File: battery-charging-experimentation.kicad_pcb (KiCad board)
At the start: 2 copper layers, 37 x 22.5 mm, 21 parts, among them J1 USB_C_Receptacle_PowerOnly_6P, Q1 FS8205A, Q2 AO3415A, U2 DW01, U3 TP4056-42-ESOP8

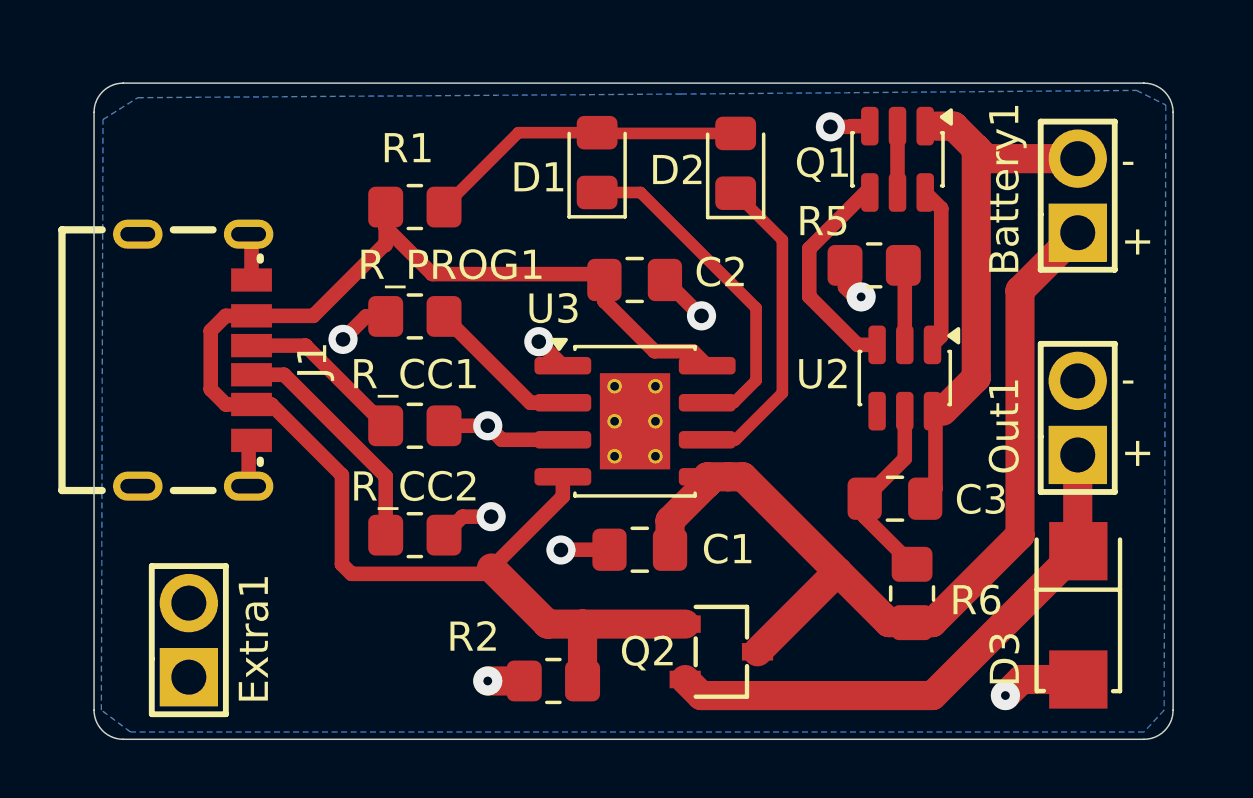
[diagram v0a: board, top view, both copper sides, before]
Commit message: move diode so the thing actually works
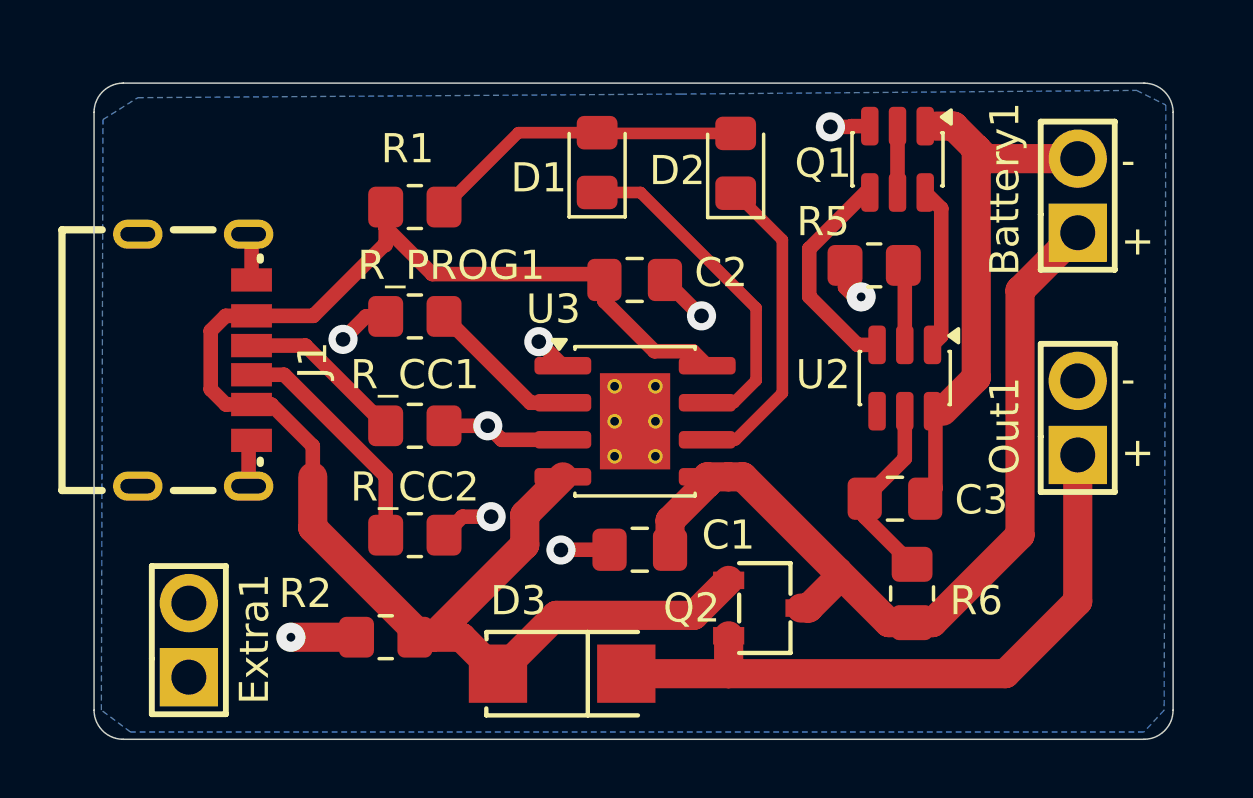
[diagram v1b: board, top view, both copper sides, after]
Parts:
- moved D3 17.8 mm to (69.5, 67.8), turned to 180 degrees
- moved R2 5.94 mm to (63.5, 66.5)
- moved Q2 2.11 mm to (76.5, 65.5)
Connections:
- D3 pad 2: GND -> /VBUS
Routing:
- net /VBUS: track 52.3 -> 57.5 mm
- net /VBUS or BATT+: track 19.1 -> 22.8 mm
- net BATT+: track 32.1 -> 30.2 mm
- net GND: track 22.5 -> 20.8 mm, vias 10 -> 9

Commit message: add a vbus out pin
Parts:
- Out1: footprint easyeda2kicad:HDR-TH_2P-P2.54-V-M -> Connector_PinHeader_2.54mm:PinHeader_1x03_P2.54mm_Vertical
- moved Out1 1.27 mm to (87.2, 60.2), turned to 0 degrees
- moved D3 0.87 mm to (70.0, 67.0)
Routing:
- net /VBUS: track 57.5 -> 78.5 mm
- net /VBUS or BATT+: track 22.8 -> 20.9 mm
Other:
- board text added: "B"
- board text added: "chargey board v2.0"
- board text removed: "chargey board v1.0"

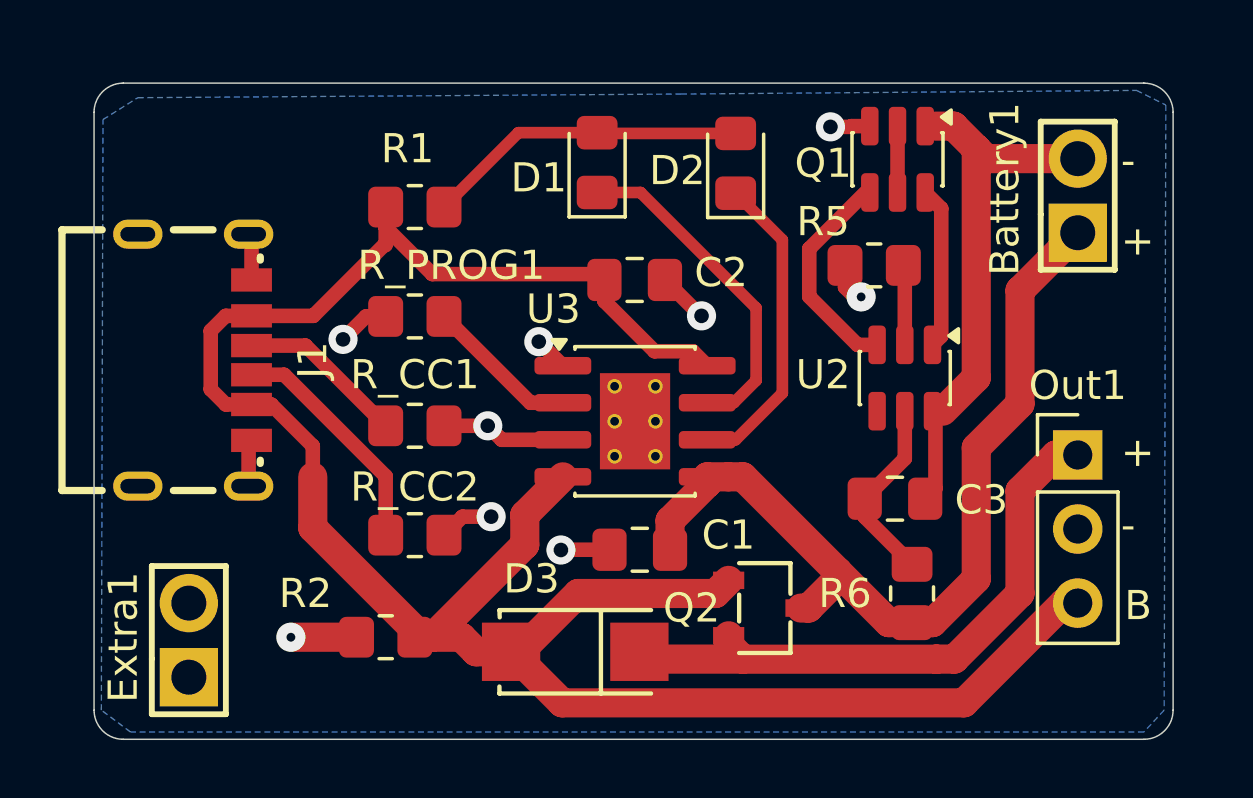
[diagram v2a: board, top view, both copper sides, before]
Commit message: smaller components, power from pico USB port
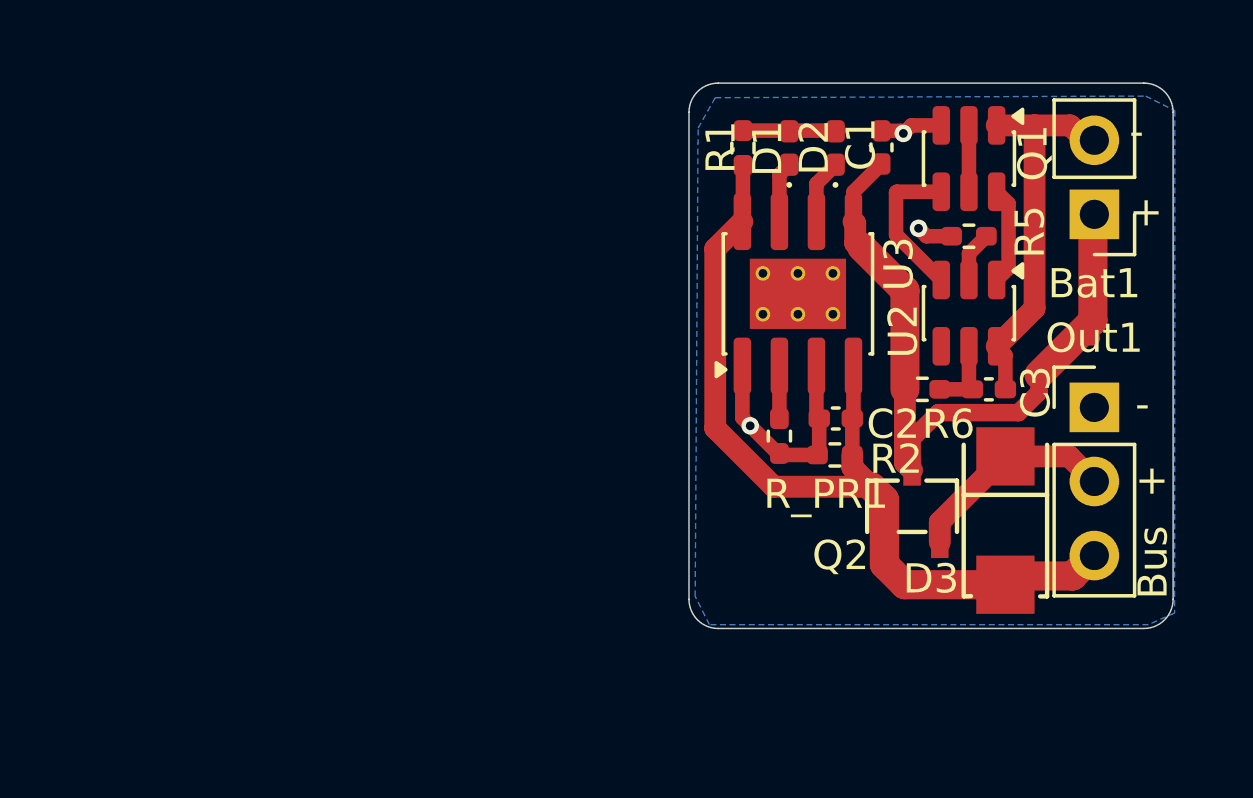
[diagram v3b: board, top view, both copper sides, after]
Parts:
- removed Battery1, Extra1: Header, easyeda2kicad:HDR-TH_2P-P2.54-V-M
- removed J1: USB_C_Receptacle_PowerOnly_6P, easyeda2kicad:USB-C-SMD
- removed R_CC1, R_CC2: 5.1k, Resistor_SMD:R_0805_2012Metric_Pad1.20x1.40mm_HandSolder
- removed R_PROG1: 1.2k, Resistor_SMD:R_0805_2012Metric_Pad1.20x1.40mm_HandSolder
- added Bat1: Conn_01x02_Pin, Connector_PinHeader_2.54mm:PinHeader_1x02_P2.54mm_Vertical, F.Cu at (87.8, 52.0)
- added R_PR1: 1.2k, Resistor_SMD:R_0402_1005Metric_Pad0.72x0.64mm_HandSolder, F.Cu at (77.0, 59.6)
- C1, C2, C3: footprint Capacitor_SMD:C_0805_2012Metric_Pad1.18x1.45mm_HandSolder -> Capacitor_SMD:C_0402_1005Metric_Pad0.74x0.62mm_HandSolder
- D1, D2: footprint LED_SMD:LED_0805_2012Metric_Pad1.15x1.40mm_HandSolder -> LED_SMD:LED_0402_1005Metric_Pad0.77x0.64mm_HandSolder
- R1, R2, R5, R6: footprint Resistor_SMD:R_0805_2012Metric_Pad1.20x1.40mm_HandSolder -> Resistor_SMD:R_0402_1005Metric_Pad0.72x0.64mm_HandSolder
- moved R2 16.6 mm to (78.9, 60.2)
- moved C1 16.1 mm to (80.5, 49.7), turned to 90 degrees
- moved D3 15.4 mm to (84.8, 62.5), turned to -90 degrees
- moved R1 11.4 mm to (75.8, 49.7), turned to -90 degrees
- moved C2 8.37 mm to (78.9, 59.0), turned to 180 degrees
- moved U3 7.09 mm to (77.6, 54.7), turned to 90 degrees
- moved R6 7.01 mm to (81.9, 58.0), turned to 0 degrees
- moved D1 6.61 mm to (77.3, 49.7)
- moved Q2 6.14 mm to (81.5, 62.0), turned to -90 degrees
- moved C3 4.94 mm to (84.2, 58.0)
- moved D2 3.46 mm to (78.9, 49.7)
- moved R5 3.40 mm to (83.5, 52.8)
- moved U2 3.13 mm to (83.5, 55.4)
- moved Q1 2.45 mm to (83.5, 50.1)
- moved Out1 1.73 mm to (87.8, 58.6)
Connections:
- Out1 pad 1: /VBUS or BATT+ -> GND
- Out1 pad 2: GND -> /VBUS or BATT+
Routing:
- net /VBUS: track 78.5 -> 30.6 mm
- net /VBUS or BATT+: track 20.9 -> 7.29 mm
- net Net-(D1-K): track 11.6 -> 2.09 mm
- net GND: track 20.8 -> 11.4 mm, vias 9 -> 3
- net Net-(D2-K): track 10.8 -> 2.25 mm
- net Net-(J1-CC2): track 8.06 -> 0.00 mm
- net Net-(D1-A): track 11.1 -> 3.18 mm
- net Net-(J1-CC1): track 5.74 -> 0.00 mm
- net /Raw Bat -: track 18.3 -> 13.3 mm
- net Net-(U2-VDD): track 6.49 -> 2.64 mm
- net Net-(U3-PROG): track 5.30 -> 1.85 mm
- net BATT+: track 30.2 -> 27.2 mm
- net /Charge control: track 7.53 -> 5.20 mm
- net /Discharge control: track 5.58 -> 3.36 mm
- net Net-(U2-CSI): track 2.50 -> 1.75 mm
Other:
- board size 37 x 22.5 mm -> 16.6 x 18.7 mm
- board text added: "Bus"
- board text removed: "B"

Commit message: put the usb port on smol version
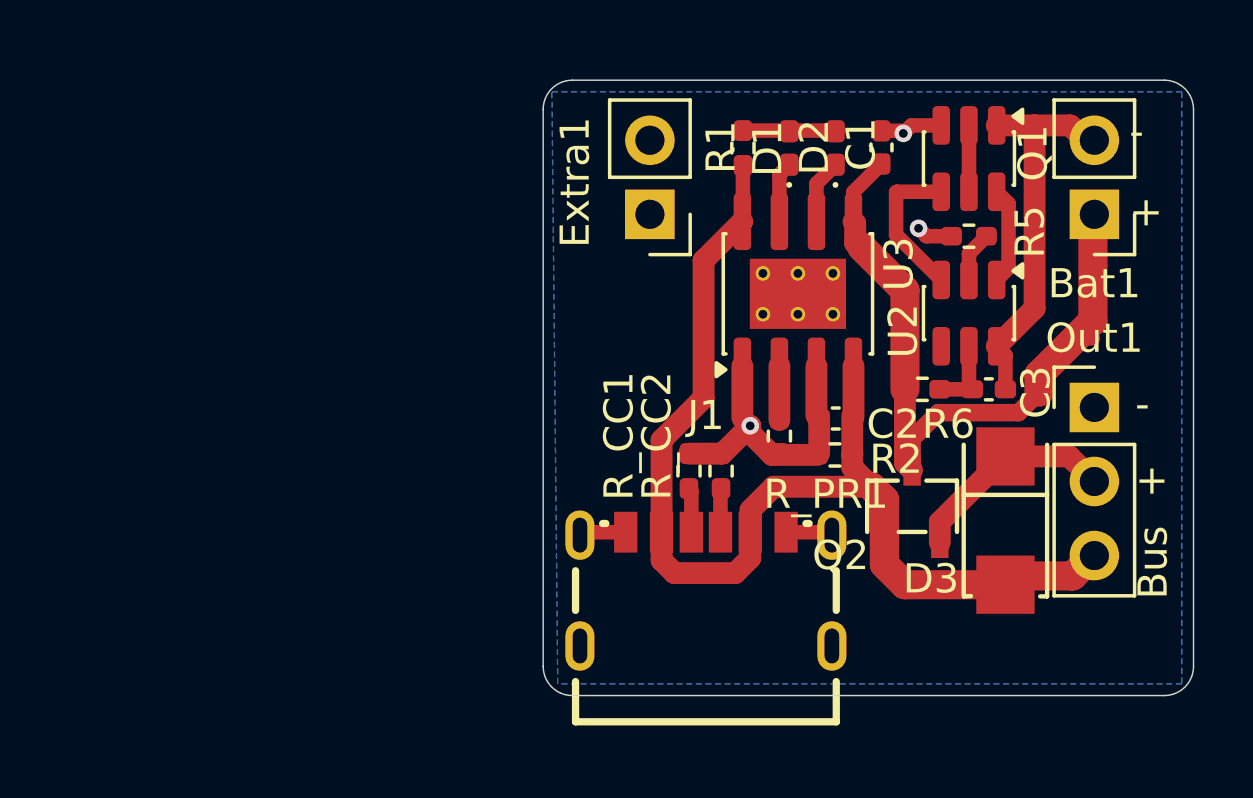
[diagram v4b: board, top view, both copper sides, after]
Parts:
- added Extra1: Conn_01x02_Pin, Connector_PinHeader_2.54mm:PinHeader_1x02_P2.54mm_Vertical, F.Cu at (72.6, 52.0)
- added J1: USB_C_Receptacle_PowerOnly_6P, easyeda2kicad:USB-C-SMD, F.Cu at (74.5, 64.8)
- added R_CC1: 5.1k, Resistor_SMD:R_0402_1005Metric_Pad0.72x0.64mm_HandSolder, F.Cu at (73.9, 60.8)
- added R_CC2: 5.1k, Resistor_SMD:R_0402_1005Metric_Pad0.72x0.64mm_HandSolder, F.Cu at (75.0, 60.8)
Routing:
- net /VBUS: track 30.6 -> 39.2 mm
- net GND: track 11.4 -> 17.3 mm
- net Net-(J1-CC1): track 0.00 -> 1.53 mm
- net Net-(J1-CC2): track 0.00 -> 1.51 mm
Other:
- board size 16.6 x 18.7 mm -> 22.3 x 21.1 mm

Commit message: update lcsc parts (double check before ordering though)
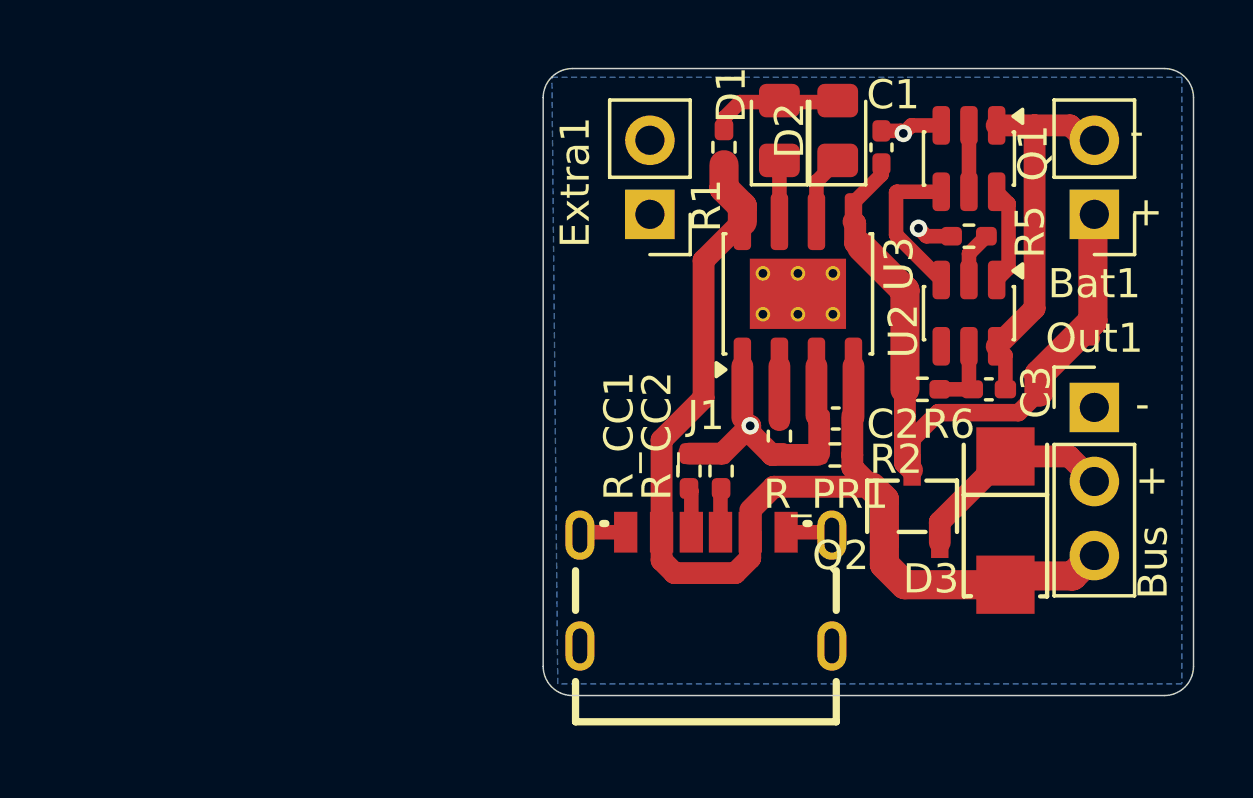
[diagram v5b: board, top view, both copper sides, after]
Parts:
- D1, D2: footprint LED_SMD:LED_0402_1005Metric_Pad0.77x0.64mm_HandSolder -> LED_SMD:LED_0805_2012Metric_Pad1.15x1.40mm_HandSolder
- moved D1 0.69 mm to (77.0, 49.1)
- moved R1 0.65 mm to (75.1, 49.7)
- moved D2 0.60 mm to (79.0, 49.1)
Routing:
- net Net-(D1-A): track 3.18 -> 4.53 mm
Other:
- board size 22.3 x 21.1 mm -> 22.3 x 21.5 mm

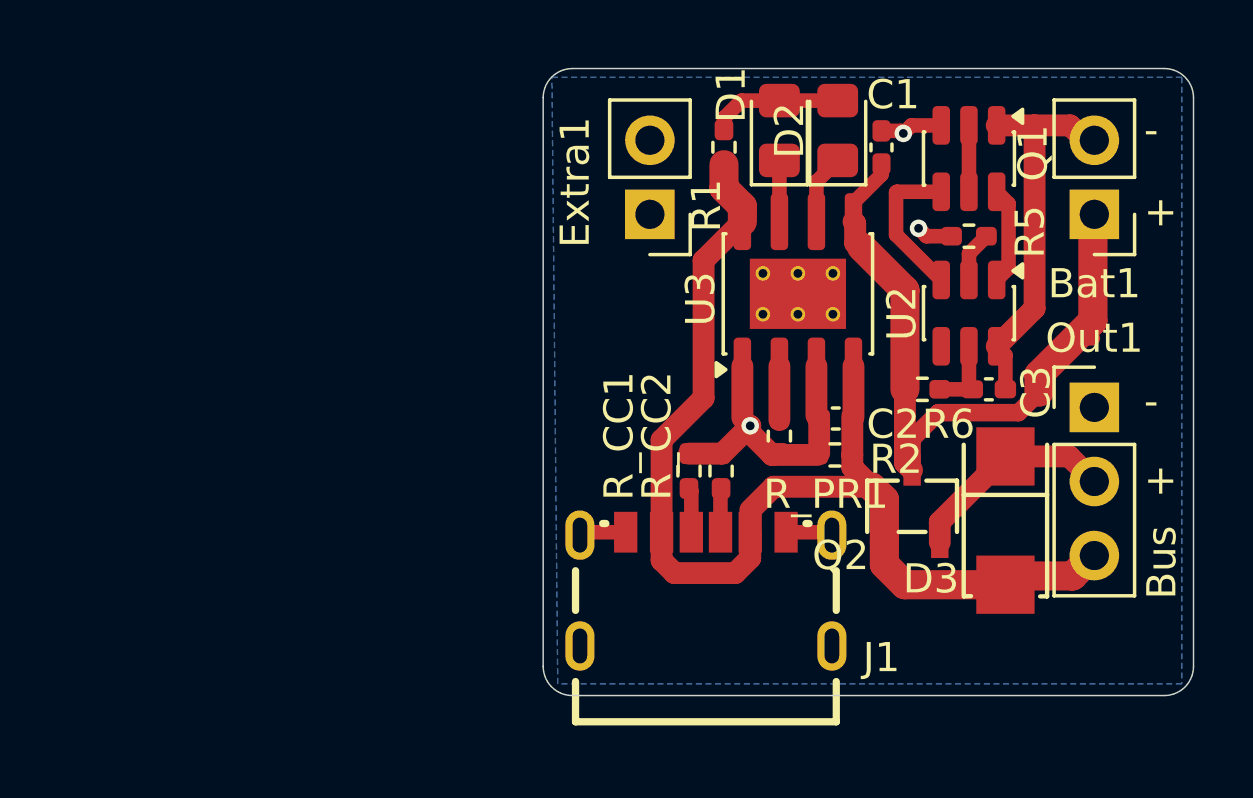
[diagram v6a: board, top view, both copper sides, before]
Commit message: update bom and clean up silkscreen
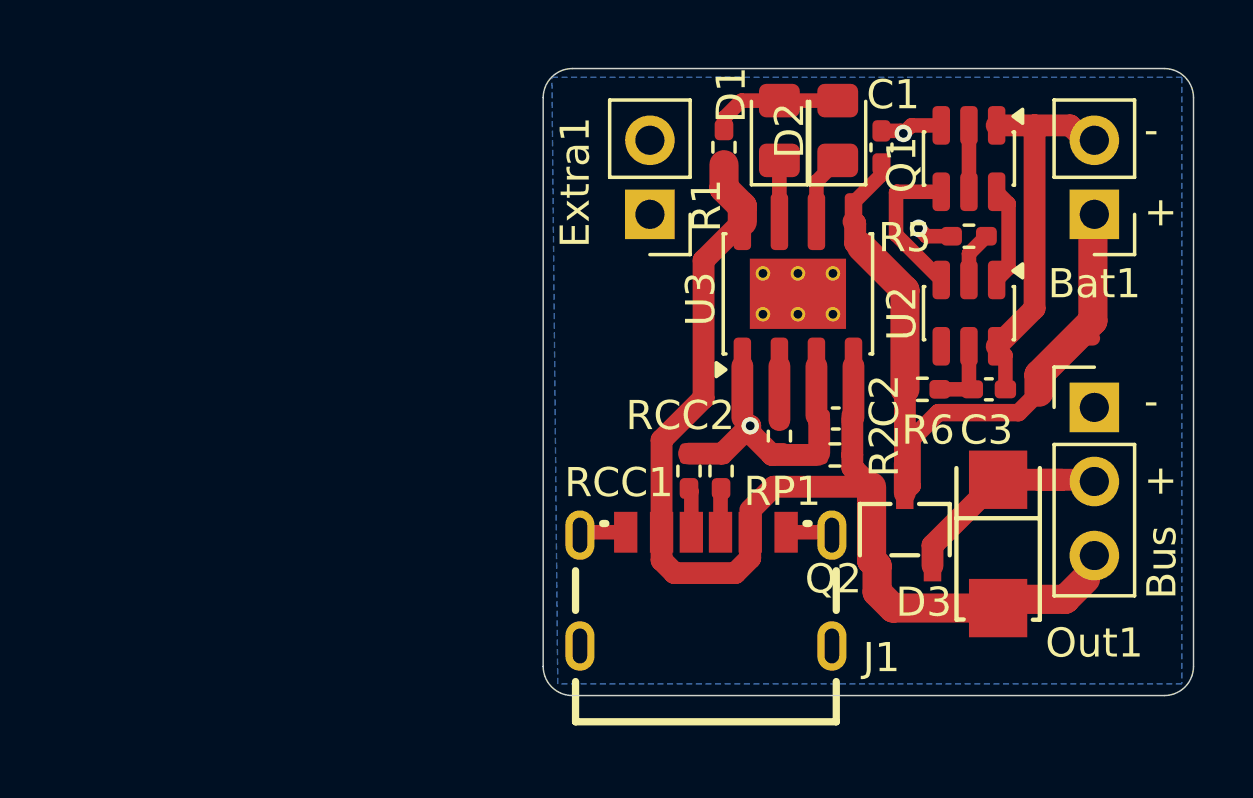
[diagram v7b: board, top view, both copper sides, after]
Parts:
- moved Q2 0.84 mm to (81.3, 62.8)
- moved D3 0.84 mm to (84.5, 63.3)
- renumbered R_CC1 to RCC1, R_CC2 to RCC2, R_PR1 to RP1
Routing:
- net BATT+: track 27.2 -> 28.8 mm
- net /VBUS: track 39.6 -> 40.4 mm
- net /VBUS or BATT+: track 7.29 -> 8.00 mm
